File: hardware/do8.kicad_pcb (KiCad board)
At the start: 4 copper layers, 100 x 85 mm, 116 parts, among them J101 TNG-Power-TOP, J102 TNG-Power-BTM, J103 TNG-Data-TOP, J104 TNG-Data-BTM, P102 Debug, P103 PE, P201 OUTPUT0, P202 OUTPUT1, P203 OUTPUT2, P204 OUTPUT3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

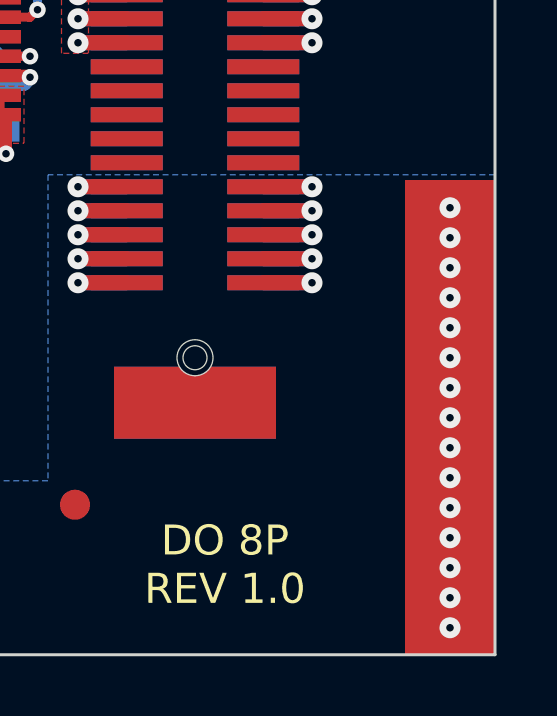
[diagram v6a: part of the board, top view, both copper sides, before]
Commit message: add hook footprint
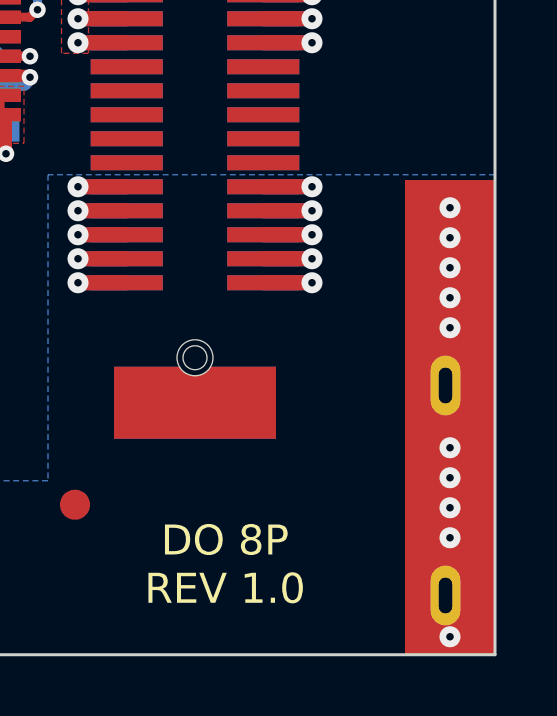
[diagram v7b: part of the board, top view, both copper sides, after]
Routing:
- net Earth: track 54.1 -> 54.4 mm, vias 31 -> 26
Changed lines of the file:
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@@
     (thickness 1.6)
     (drawings 30)
-    (tracks 1830)
+    (tracks 1825)
     (zones 0)
     (modules 116)
@@
     (add_net USB-DPC)
   )
+  (module kicad-libraries:PE_Hook (layer F.Cu)
+    (at 188.3 139.6)
+    (fp_text reference P103 (at 0 0.5) (layer F.Fab)
+      (effects (font (size 0.15 0.15) (thickness 0.0375)))
+    )
+    (fp_text value PE (at 0 -0.5) (layer F.Fab)
+      (effects (font (size 0.15 0.15) (thickness 0.0375)))
+    )
+    (pad 1 thru_hole oval (at -0.15 -1.075) (size 1 2) (drill oval 0.45 1.2) (layers *.Cu *.Mask)
+      (net 12 Earth))
+    (pad 1 thru_hole oval (at -0.15 5.925) (size 1 2) (drill oval 0.45 1.2) (layers *.Cu *.Mask)
+      (net 12 Earth))
+    (pad 1 smd rect (at 0 0) (size 3 15.85) (layers F.Cu)
+      (net 12 Earth))
+    (model Connectors_TF/PE_Hook.wrl
+      (at (xyz 0 0 0))
+      (scale (xyz 1 1 1))
+      (rotate (xyz 0 0 0))
+    )
+  )
   (module kicad-libraries:WE-SL5 (layer F.Cu)
     (at 150.5 135.65 180)
@@
       (clearance 0.65024))
   )
-  (module kicad-libraries:PE_Hook (layer F.Cu)
-    (at 188.3 139.6)
-    (fp_text reference P103 (at 0 0.5) (layer F.Fab)
-      (effects (font (size 0.15 0.15) (thickness 0.0375)))
-    )
-    (fp_text value PE (at 0 -0.5) (layer F.Fab)
-      (effects (font (size 0.15 0.15) (thickness 0.0375)))
-    )
-    (pad 1 smd rect (at 0 0) (size 3 15.85) (layers B.Cu B.Paste B.Mask)
-      (net 12 Earth))
-    (pad 1 smd rect (at 0 0) (size 3 15.85) (layers F.Cu F.Paste F.Mask)
-      (net 12 Earth))
-  )
   (module kicad-libraries:TEL10 (layer F.Cu)
     (at 133.15 135.25 180)
@@
   (via (at 175.9 135.1) (size 0.7) (drill 0.25) (layers F.Cu B.Cu) (net 12))
   (segment (start 175.9 135.1) (end 177.525 135.1) (width 0.5) (layer F.Cu) (net 12) (status 800000))
-  (via (at 188.3 139.6) (size 0.7) (drill 0.25) (layers F.Cu B.Cu) (net 12))
-  (via (at 188.3 138.6) (size 0.7) (drill 0.25) (layers F.Cu B.Cu) (net 12))
   (segment (start 188.3 139.6) (end 188.3 138.6) (width 0.7) (layer F.Cu) (net 12))
-  (via (at 188.3 137.6) (size 0.7) (drill 0.25) (layers F.Cu B.Cu) (net 12))
   (segment (start 188.3 139.6) (end 188.3 137.6) (width 0.7) (layer F.Cu) (net 12))
   (via (at 188.3 136.6) (size 0.7) (drill 0.25) (layers F.Cu B.Cu) (net 12))
@@
   (via (at 188.3 143.6) (size 0.7) (drill 0.25) (layers F.Cu B.Cu) (net 12))
   (segment (start 188.3 142.6) (end 188.3 143.6) (width 0.7) (layer B.Cu) (net 12))
-  (via (at 188.3 144.6) (size 0.7) (drill 0.25) (layers F.Cu B.Cu) (net 12))
   (segment (start 188.3 143.6) (end 188.3 144.6) (width 0.7) (layer F.Cu) (net 12))
-  (via (at 188.3 145.6) (size 0.7) (drill 0.25) (layers F.Cu B.Cu) (net 12))
   (segment (start 188.3 144.6) (end 188.3 145.6) (width 0.7) (layer B.Cu) (net 12))
-  (via (at 188.3 146.6) (size 0.7) (drill 0.25) (layers F.Cu B.Cu) (net 12))
-  (segment (start 188.3 145.6) (end 188.3 146.6) (width 0.7) (layer F.Cu) (net 12))
   (via (at 188.3 135.6) (size 0.7) (drill 0.25) (layers F.Cu B.Cu) (net 12))
   (segment (start 188.3 136.6) (end 188.3 135.6) (width 0.7) (layer B.Cu) (net 12))
@@
   (segment (start 131.5 143.8) (end 132.2 144.5) (width 0.7) (layer F.Cu) (net 12))
   (segment (start 132.2 144.5) (end 132.3 144.5) (width 0.7) (layer F.Cu) (net 12))
+  (segment (start 188.3 145.6) (end 188.3 146.9) (width 0.7) (layer F.Cu) (net 12))
+  (via (at 188.3 146.9) (size 0.7) (drill 0.25) (layers F.Cu B.Cu) (net 12))
   (segment (start 102.6 142.9) (end 95.94982 142.9) (width 0.7) (layer GND) (net 13) (status 800000))
   (segment (start 95.94982 142.9) (end 95.8 142.75018) (width 0.7) (layer GND) (net 13) (status C00000))
